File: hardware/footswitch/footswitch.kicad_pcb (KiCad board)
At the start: 2 copper layers, 39 x 24 mm, 2 parts, among them J1 Conn_02x05_Counter_Clockwise

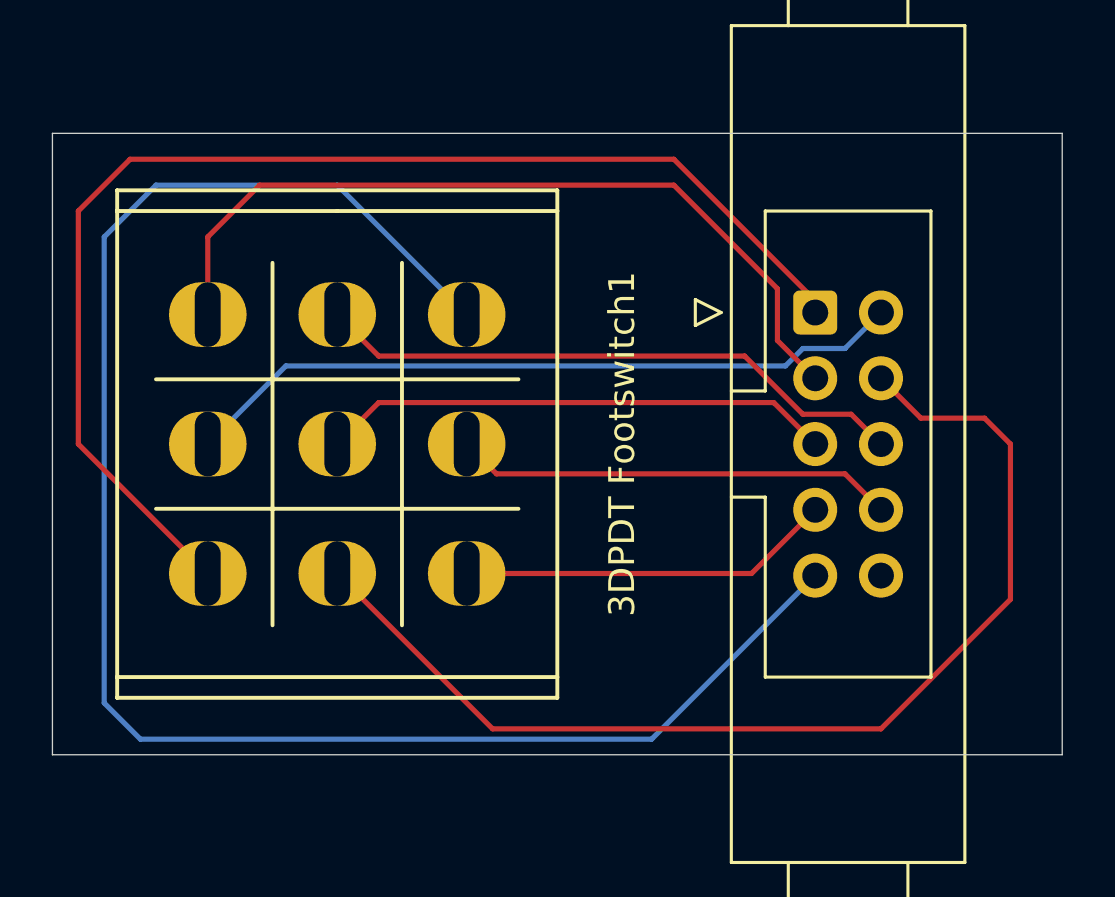
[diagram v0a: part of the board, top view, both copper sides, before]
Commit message: Wider traces for footswitch PCB and connect main board
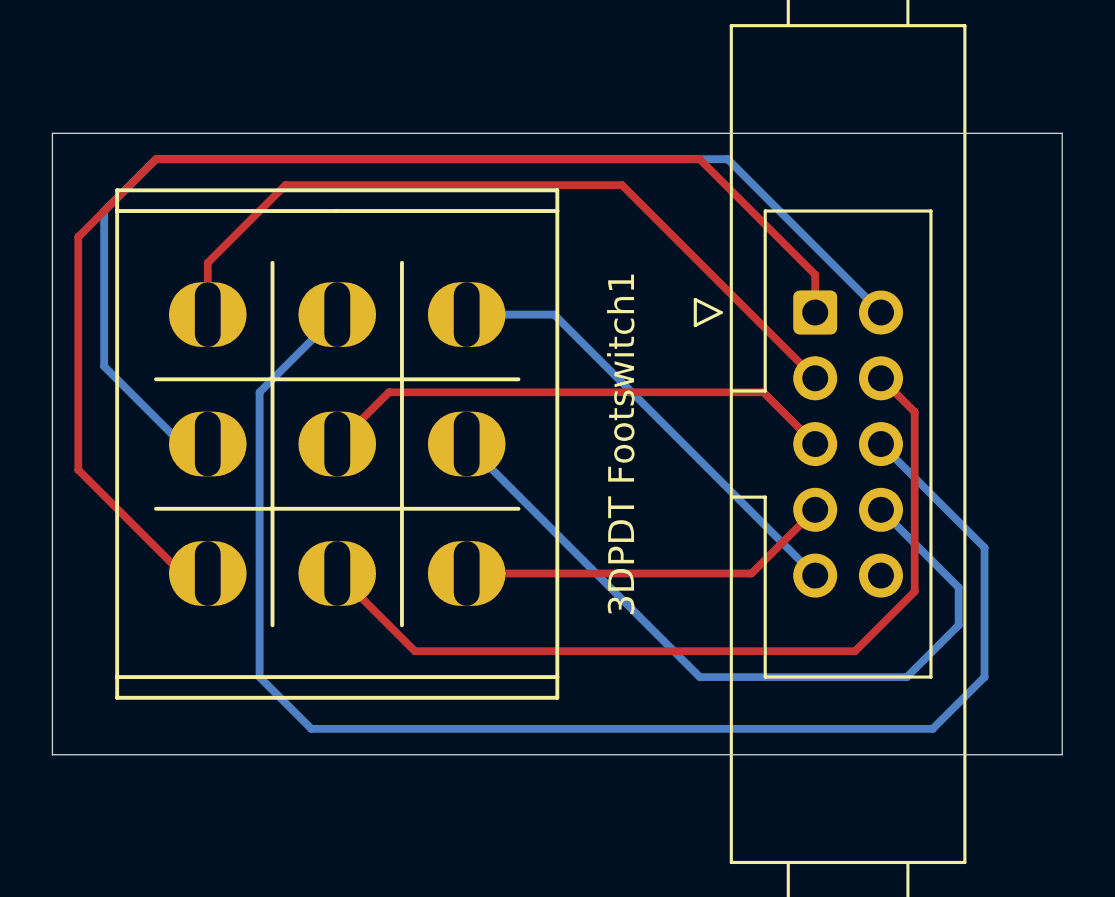
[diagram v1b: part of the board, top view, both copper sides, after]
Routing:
- net /conn9: track 65.6 -> 17.6 mm
- net /conn6: track 23.1 -> 55.6 mm
- net /conn2: track 28.1 -> 44.5 mm
- net /conn8: track 17.1 -> 29.3 mm
- net /conn4: track 42.6 -> 33.3 mm
- net /conn3: track 31.6 -> 29.8 mm
- net /conn1: track 48.1 -> 48.7 mm

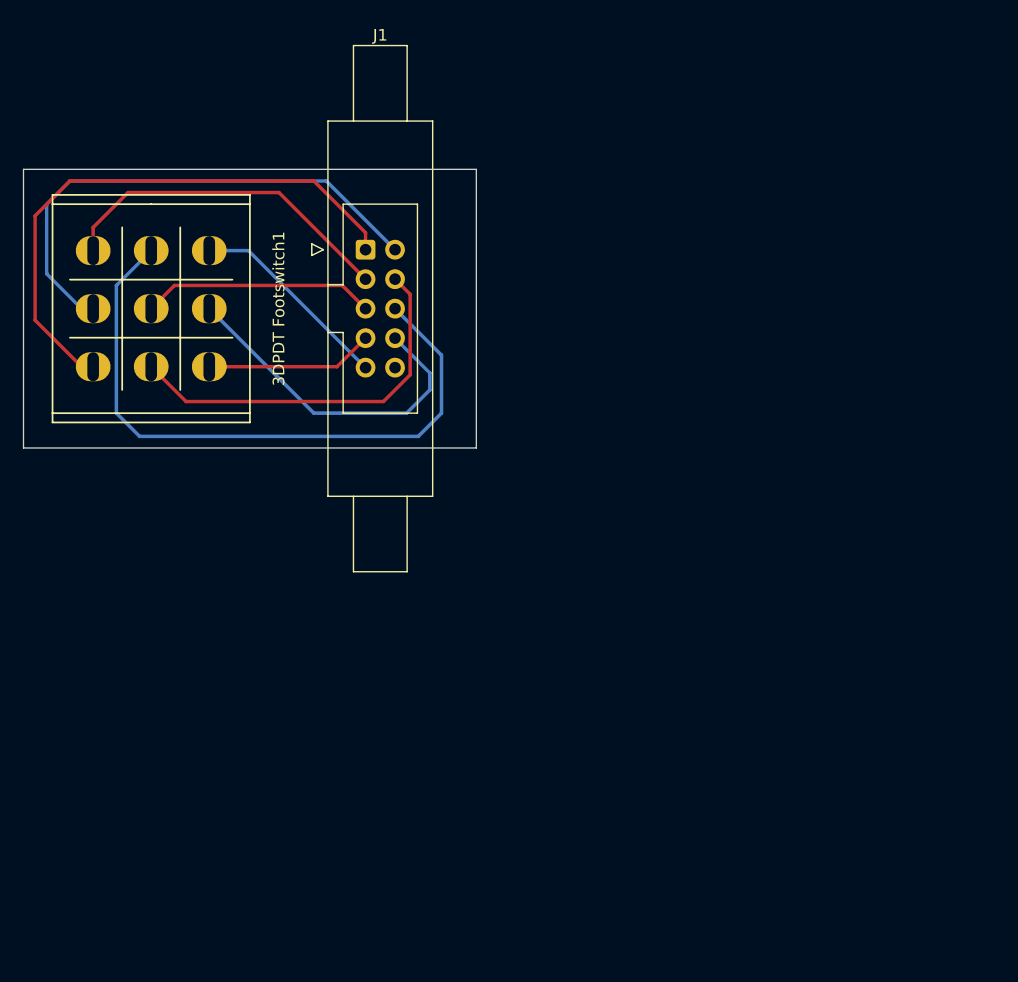
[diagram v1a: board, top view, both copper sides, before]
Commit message: Resize footswitch board, adjust footprints
Resistor and diode added
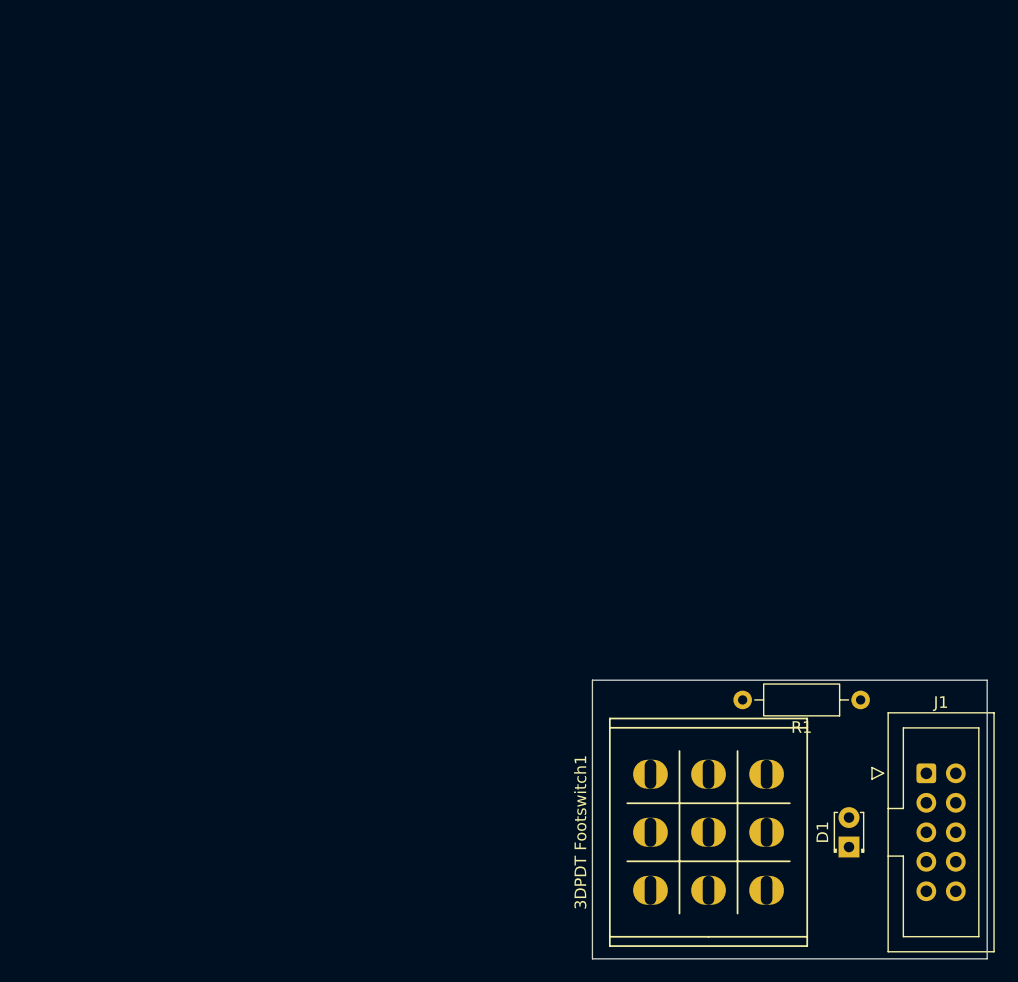
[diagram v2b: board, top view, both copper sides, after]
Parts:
- added D1: LED, LED_THT:LED_D1.8mm_W3.3mm_H2.4mm, F.Cu at (152.1, 113.4)
- added R1: 1k, Resistor_THT:R_Axial_DIN0207_L6.3mm_D2.5mm_P10.16mm_Horizontal, F.Cu at (153.1, 100.7)
- J1: footprint Connector_IDC:IDC-Header_2x05_P2.54mm_Latch6.5mm_Vertical -> Connector_IDC:IDC-Header_2x05_P2.54mm_Vertical
- moved J1 66.1 mm to (158.8, 107.0)
- moved 3DPDT Footswitch1 65.9 mm to (140.0, 112.1), turned to -90 degrees
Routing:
- net /conn6: track 55.6 -> 0.00 mm
- net /conn1: track 48.7 -> 0.00 mm
- net /conn2: track 44.5 -> 0.00 mm
- net /conn4: track 33.3 -> 0.00 mm
- net /conn3: track 29.8 -> 0.00 mm
- net /conn8: track 29.3 -> 0.00 mm
- net /conn5: track 20.1 -> 0.00 mm
- net /conn9: track 17.6 -> 0.00 mm
- net /conn7: track 14.5 -> 0.00 mm
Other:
- board size 39 x 24 mm -> 34 x 24 mm

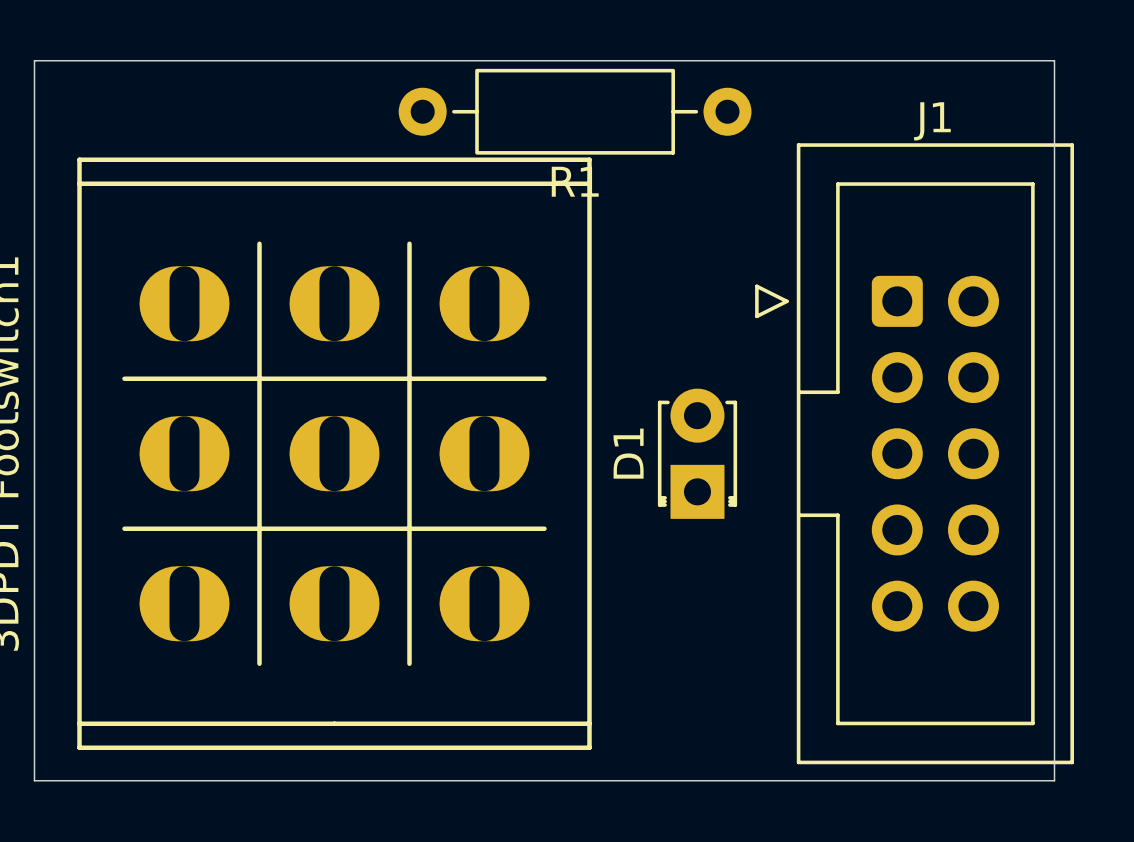
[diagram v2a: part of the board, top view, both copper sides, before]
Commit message: Connect everything with traces
Corrected schematic with fsw2
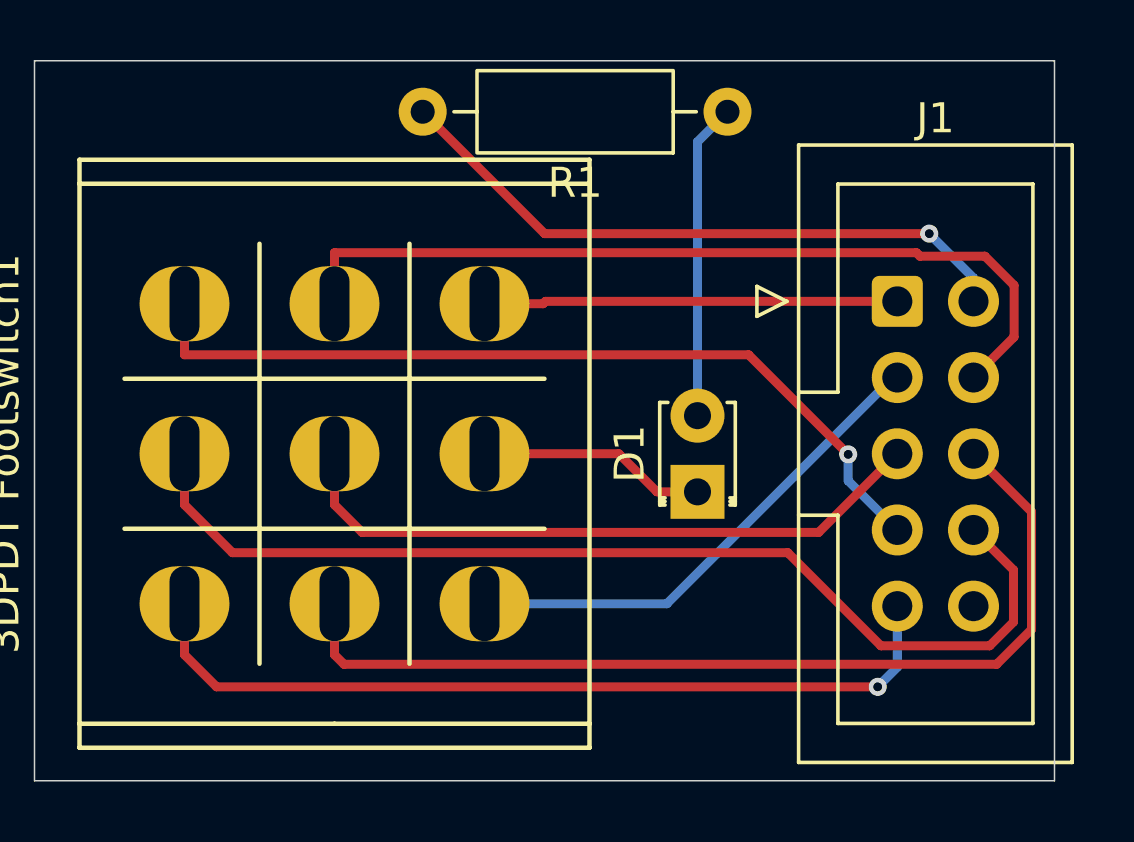
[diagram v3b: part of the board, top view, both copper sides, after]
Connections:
- 3DPDT Footswitch1 pad 2: /conn2 -> /fsw2
- D1 pad 1: /conn2 -> /fsw2
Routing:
- net /conn8: track 0.00 -> 35.2 mm
- net /conn6: track 0.00 -> 32.2 mm
- net /conn4: track 0.00 -> 28.4 mm
- net /conn7: track 0.00 -> 28.4 mm, vias 0 -> 1
- net /conn9: track 0.00 -> 28.2 mm, vias 0 -> 1
- net /conn5: track 0.00 -> 21.9 mm
- net /conn2: track 0.00 -> 21.4 mm, vias 0 -> 1
- net /conn3: track 0.00 -> 16.9 mm
- net /conn1: track 0.00 -> 13.8 mm
- net Net-(D1-A): track 0.00 -> 10.5 mm
- net /fsw2: track 0.00 -> 7.63 mm
